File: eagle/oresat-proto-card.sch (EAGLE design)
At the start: 120 parts, among them J1 J-SAMTEC-TFM-110-X1-XXX-D-RA, J2 U.FL, J3 U.FL, J4 U.FL, J6 J-SAMTEC-TFM-120-X1-XXX-D-RA, J7 ORESAT-DEBUG-CONNECTOR-SOLAR, Q10 DMP2240UDM, Q2 MOSFET-PCH-SOT23-6, Q7 MOSFET-PCH-SOT23-6, Q8 PMV45EN, Q9 PMV45EN, U1 TCAN330, U10 TPS62111RSA, U11 MIC842LYC5, U12 MIC842LYC5, U2 MAX7310ATE, U6 MAX4211FETE, U7 STM32F091C, X2 16MHZ-2.5x2mm

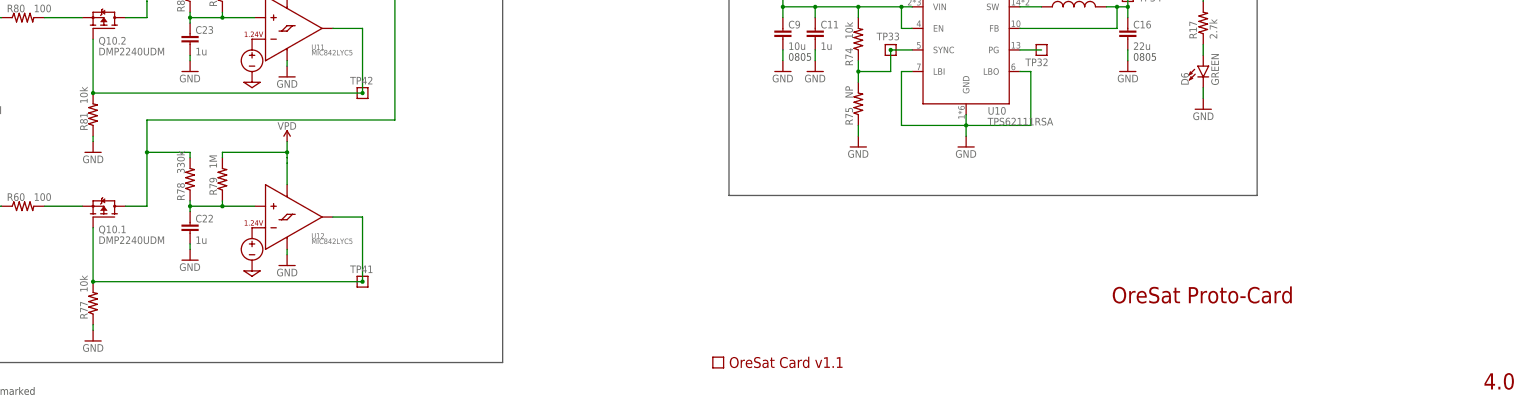
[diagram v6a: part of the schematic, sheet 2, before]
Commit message: Updated to 4.1: switched to better debug connector, fixed OPD capacitance problem.
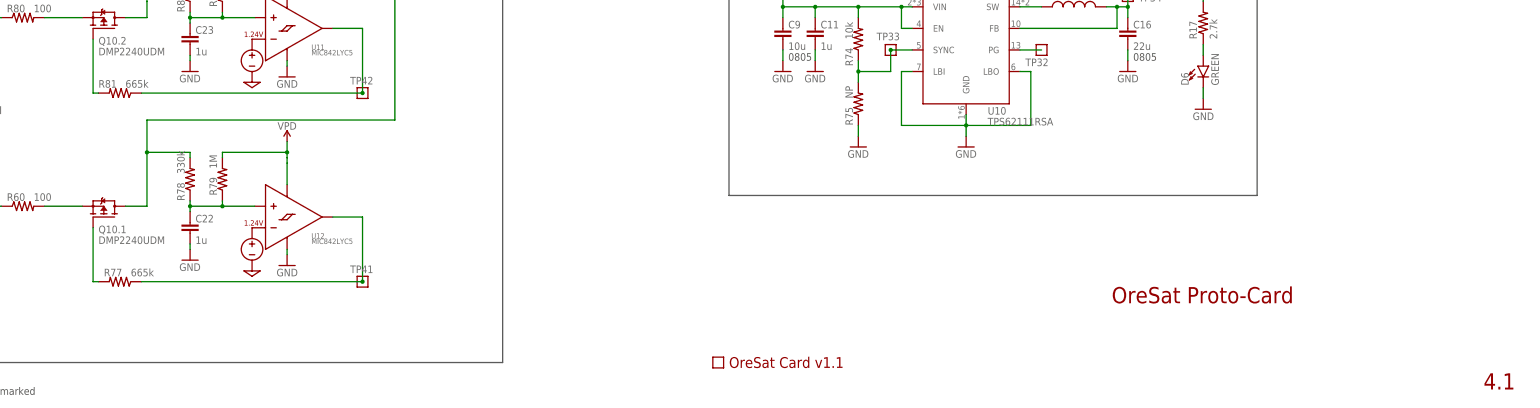
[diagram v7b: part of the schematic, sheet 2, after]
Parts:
- J7: value ORESAT-DEBUG-CONNECTOR-SOLAR -> ORESAT-DEBUG-CONNECTOR-ALL; device oresat-debug-connector:ORESAT-DEBUG-CONNECTOR-SOLAR -> oresat-debug-connector:ORESAT-DEBUG-CONNECTOR-ALL
- R77, R81: value 10k -> 665k
- TP25, TP26, TP27, TP28, TP29, TP30: value TEST-POINT -> TEST-POINT-LARGE-SQUARE; device Tova:TEST-POINT -> oresat-misc:TEST-POINT-LARGE-SQUARE
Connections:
- new net N$398: Q10.1.G, R77.2
- new net N$400: Q10.2.G, R81.2
- net GND: no longer R77.1, R81.1
- net N$539: now also R77.1; no longer Q10.1.G, R77.2
- net N$573: now also R81.1; no longer Q10.2.G, R81.2
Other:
- note added: "4.1"
- note removed: "4.0"
- moved on the sheet: R77, R81

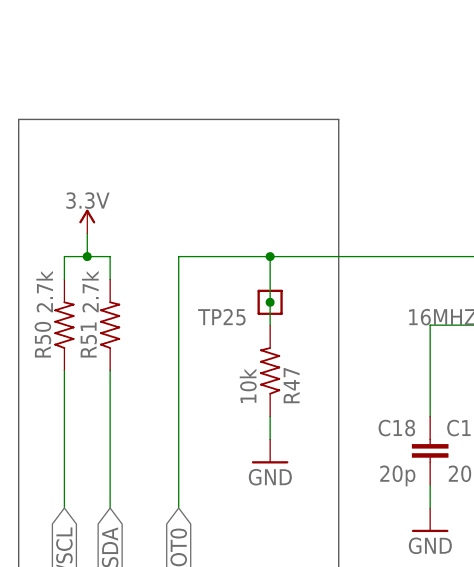
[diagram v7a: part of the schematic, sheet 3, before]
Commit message: Oh right and fix the I2C pullups to 4.7k
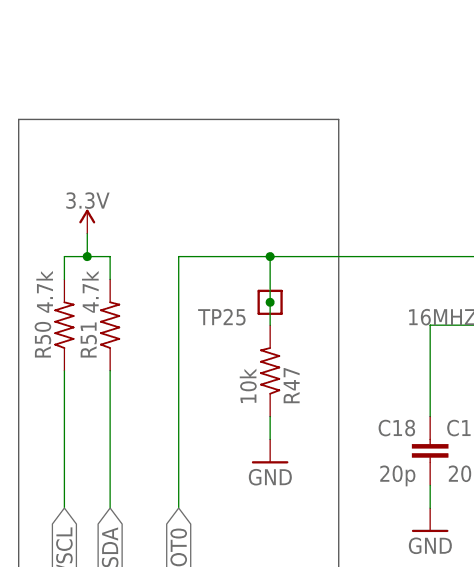
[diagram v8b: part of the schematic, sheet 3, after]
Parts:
- R50, R51: value 2.7k -> 4.7k
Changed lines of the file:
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@@
 <setting verticaltext="up"/>
 </settings>
-<grid distance="0.05" unitdist="inch" unit="inch" style="lines" multiple="1" display="no" altdistance="0.01" altunitdist="inch" altunit="inch"/>
+<grid distance="0.1" unitdist="inch" unit="inch" style="lines" multiple="1" display="no" altdistance="0.01" altunitdist="inch" altunit="inch"/>
 <layers>
 <layer number="1" name="Top" color="4" fill="1" visible="no" active="no"/>
@@
 <part name="TP29" library="oresat-misc" deviceset="TEST-POINT-LARGE-SQUARE" device=""/>
 <part name="TP30" library="oresat-misc" deviceset="TEST-POINT-LARGE-SQUARE" device=""/>
-<part name="R50" library="oresat-rcl" deviceset="R-US_" device="0603-C-NOSILK" value="2.7k">
+<part name="R50" library="oresat-rcl" deviceset="R-US_" device="0603-C-NOSILK" value="4.7k">
 <attribute name="DIS" value="Digi-Key"/>
 <attribute name="DPN" value="A129632CT-ND"/>
@@
 <attribute name="MPN" value="CRGCQ0402F2K7"/>
 </part>
-<part name="R51" library="oresat-rcl" deviceset="R-US_" device="0603-C-NOSILK" value="2.7k">
+<part name="R51" library="oresat-rcl" deviceset="R-US_" device="0603-C-NOSILK" value="4.7k">
 <attribute name="DIS" value="Digi-Key"/>
 <attribute name="DPN" value="A129632CT-ND"/>
